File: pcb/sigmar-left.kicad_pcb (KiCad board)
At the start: 2 copper layers, 137.1 x 101.7 mm, 77 parts, among them J1 AudioJack4, J2 AVR-ISP-6, SW1 Cherry-MX-LED-APA102, SW10 Cherry-MX-LED-APA102, SW11 Cherry-MX-LED-APA102, SW12 Cherry-MX-LED-APA102, SW13 Cherry-MX-LED-APA102, SW14 Cherry-MX-LED-APA102, SW15 Cherry-MX-LED-APA102, SW16 Cherry-MX-LED-APA102, SW17 Cherry-MX-LED-APA102, SW18 Cherry-MX-LED-APA102, SW19 Cherry-MX-LED-APA102, SW2 Cherry-MX-LED-APA102, SW20 Cherry-MX-LED-APA102, SW21 Cherry-MX-LED-APA102, SW22 Cherry-MX-LED-APA102, SW23 Cherry-MX-LED-APA102, SW24 Cherry-MX-LED-APA102, SW25 Cherry-MX-LED-APA102, SW26 SW_Push, SW3 Cherry-MX-LED-APA102, SW4 Cherry-MX-LED-APA102, SW5 Cherry-MX-LED-APA102, SW6 Cherry-MX-LED-APA102, SW7 Cherry-MX-LED-APA102, SW8 Cherry-MX-LED-APA102, SW9 Cherry-MX-LED-APA102, U1 ATmega32U4-AU, Y1 16MHz

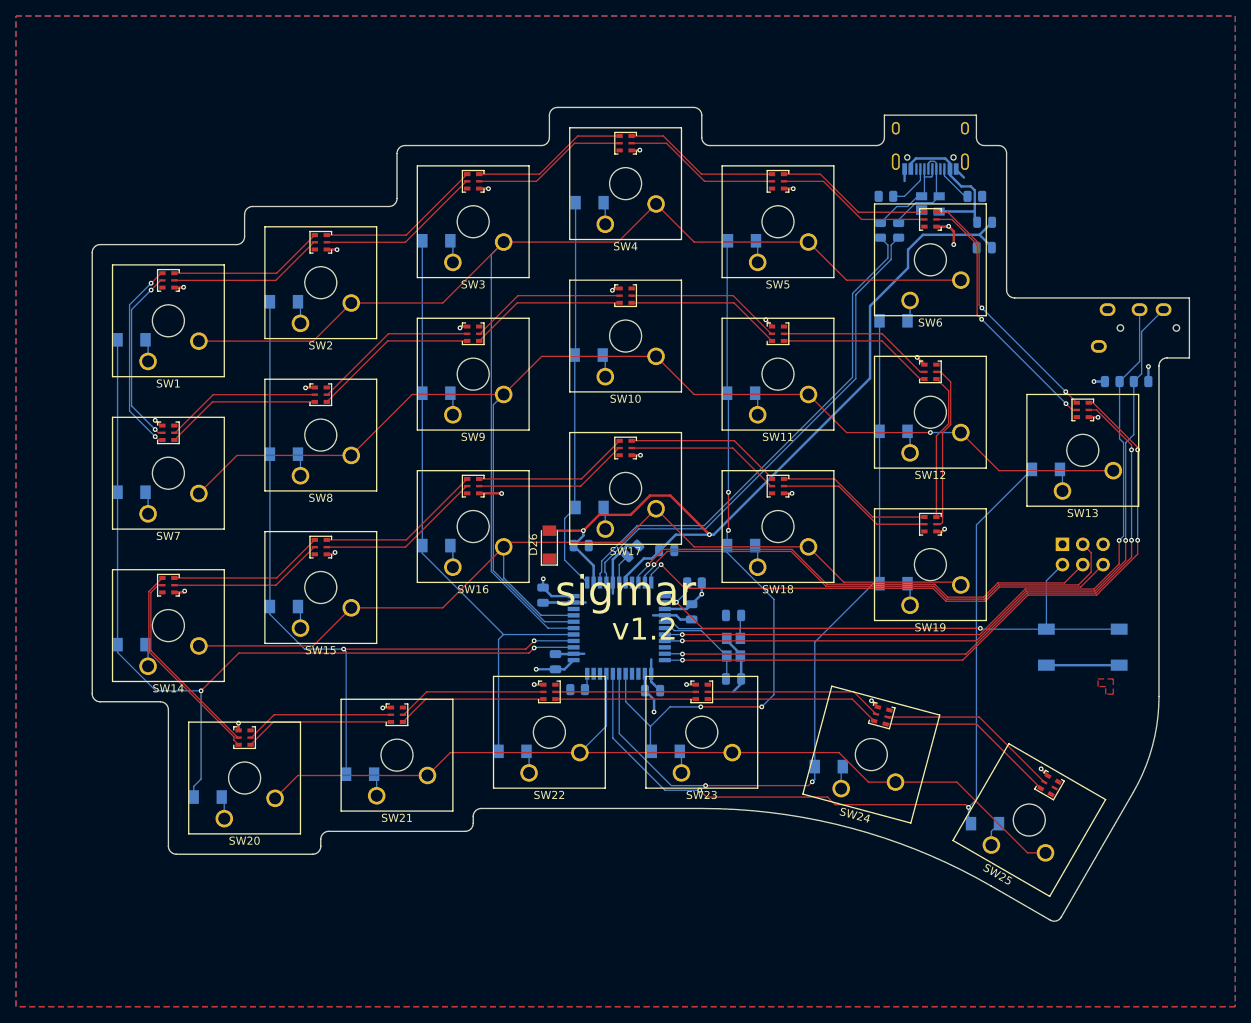
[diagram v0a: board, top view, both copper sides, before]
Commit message: make room for stabilizers
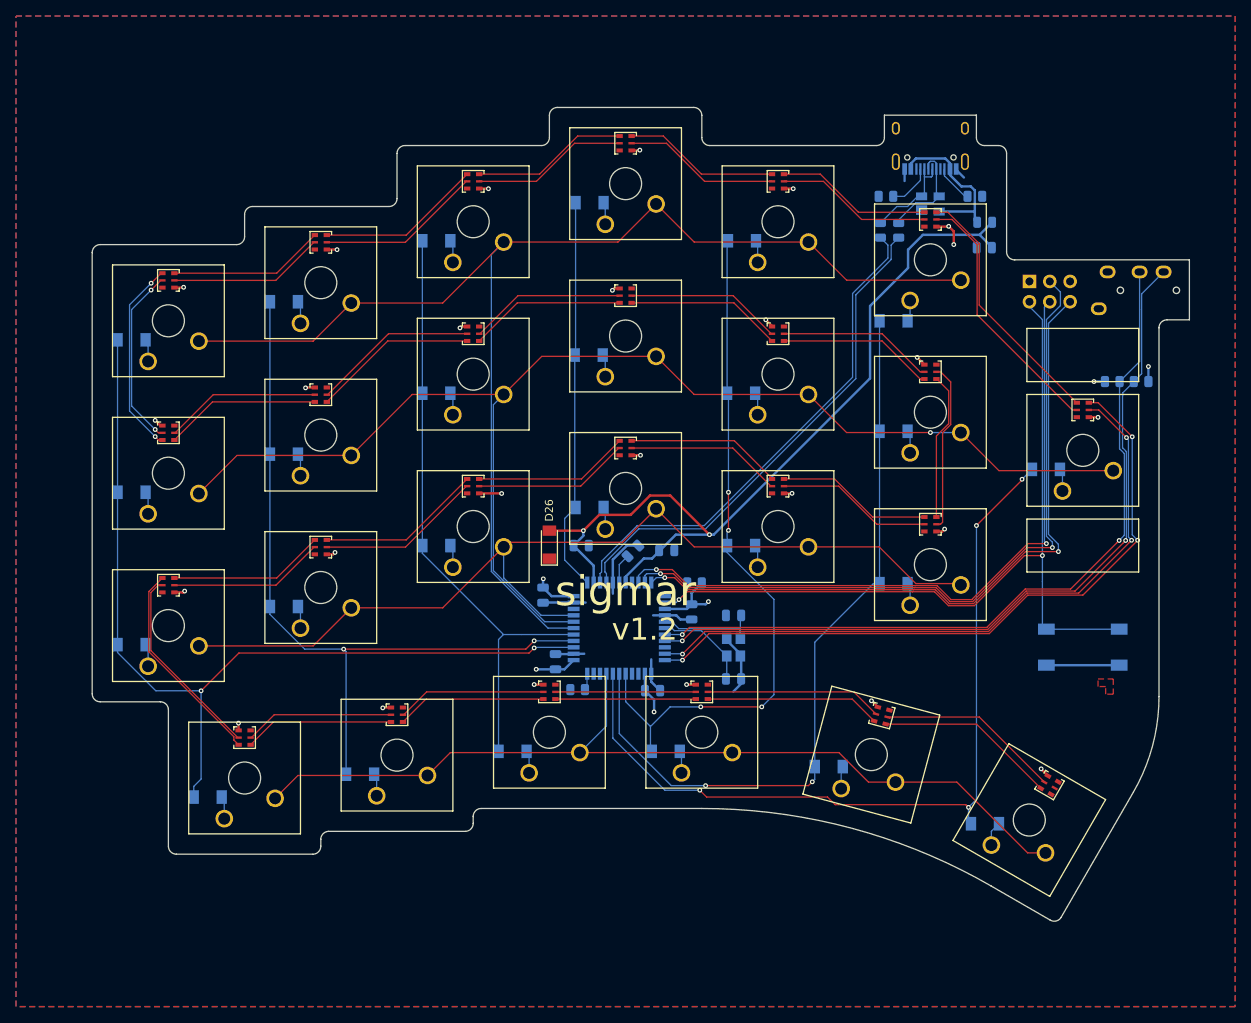
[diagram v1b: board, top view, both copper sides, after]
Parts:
- J2: value AVR-ISP-6 -> Reset_Pretty-Mask
- moved J2 33.1 mm to (208.3, 67.3)
- moved J1 4.71 mm to (225.8, 67.2)
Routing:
- net /RESET: track 70.1 -> 104.5 mm
- net /MISO: track 61.8 -> 88.1 mm, vias 1 -> 2
- net /SCK: track 62.0 -> 87.2 mm, vias 1 -> 2
- net /MOSI: track 65.8 -> 91.0 mm, vias 1 -> 2
- net /SDA: track 95.1 -> 98.7 mm
- net /SCL: track 93.7 -> 96.8 mm
- net VCC: track 25.8 -> 28.1 mm
- net /LED_CKI: track 84.6 -> 83.5 mm
- net /LED_SDI: track 86.3 -> 85.7 mm
- net /COL7: track 103.8 -> 103.9 mm, vias 2 -> 4
- net Net-(SW13-Pad7): vias 2 -> 0
- net Net-(SW13-Pad6): vias 2 -> 0
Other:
- outline, holes or cut-outs redrawn
